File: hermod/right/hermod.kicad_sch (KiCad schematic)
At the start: 36 parts, among them J1 USB_C_Receptacle_USB2.0, J2 Conn_01x05, J3 USB_C_Receptacle_USB2.0, Q1 AO3401A, Q2 MMUN2233LT1G, U1 STM32F072CBT6, U2 PRTR5V0U2X, U3 XC6206PxxxMR-Regulator_Linear, U4 CR2013-MI2120, U5 TXB0101

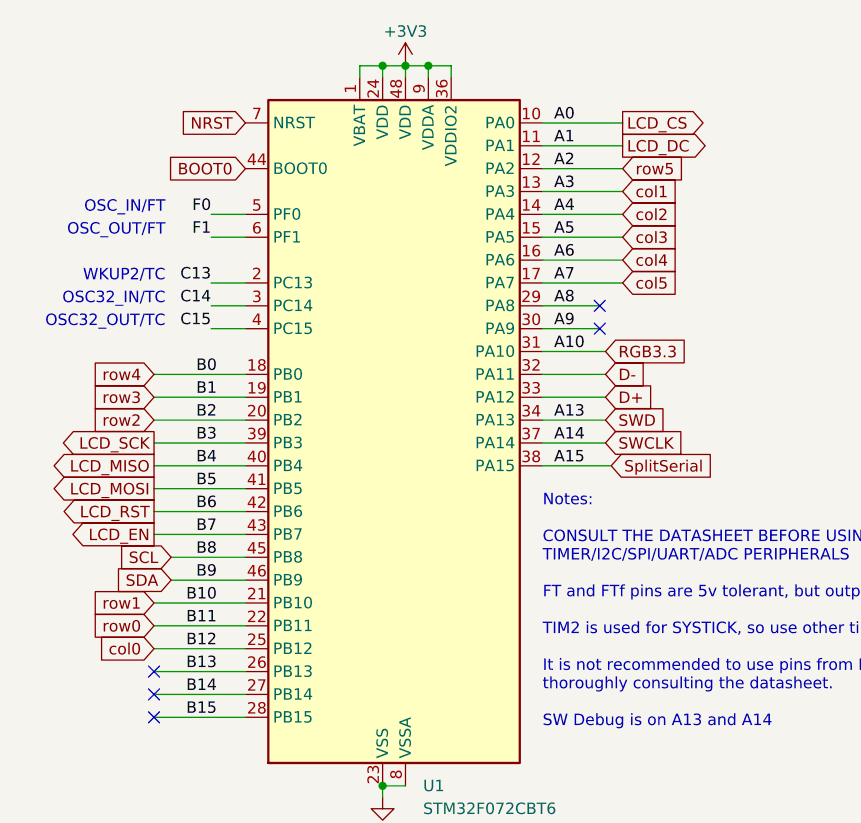
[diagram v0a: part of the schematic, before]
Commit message: Wired up rows and cols
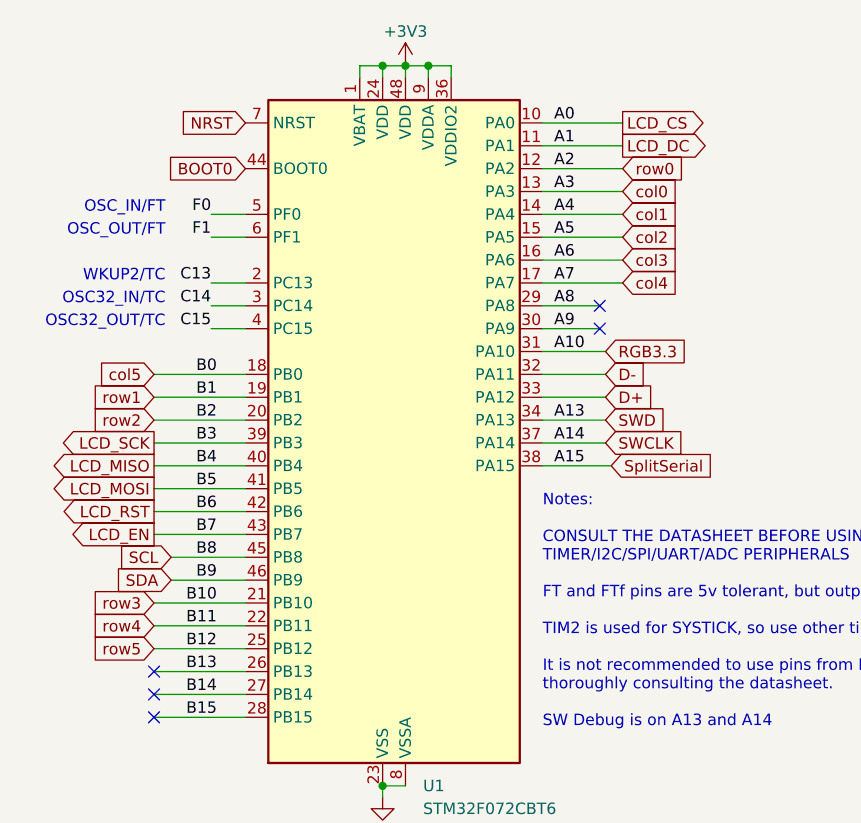
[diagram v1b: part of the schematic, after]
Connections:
- net col0: now also U1.13 (PA3); no longer U1.25 (PB12)
- net col1: now also U1.14 (PA4); no longer U1.13 (PA3)
- net col2: now also U1.15 (PA5); no longer U1.14 (PA4)
- net col3: now also U1.16 (PA6); no longer U1.15 (PA5)
- net col4: now also U1.17 (PA7); no longer U1.16 (PA6)
- net col5: now also U1.18 (PB0); no longer U1.17 (PA7)
- net row0: now also U1.12 (PA2); no longer U1.22 (PB11)
- net row1: now also U1.19 (PB1); no longer U1.21 (PB10)
- net row3: now also U1.21 (PB10); no longer U1.19 (PB1)
- net row4: now also U1.22 (PB11); no longer U1.18 (PB0)
- net row5: now also U1.25 (PB12); no longer U1.12 (PA2)
